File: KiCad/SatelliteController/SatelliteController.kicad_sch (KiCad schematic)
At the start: 35 parts, among them J1 CONN_ICSP, J13 CONN_7SEG, J2 CONN_USB, J3 USB_B_Micro, U1 FT232RL, U2 ATMEGA2560-16AUR, Y1 HUSG-16.000-20

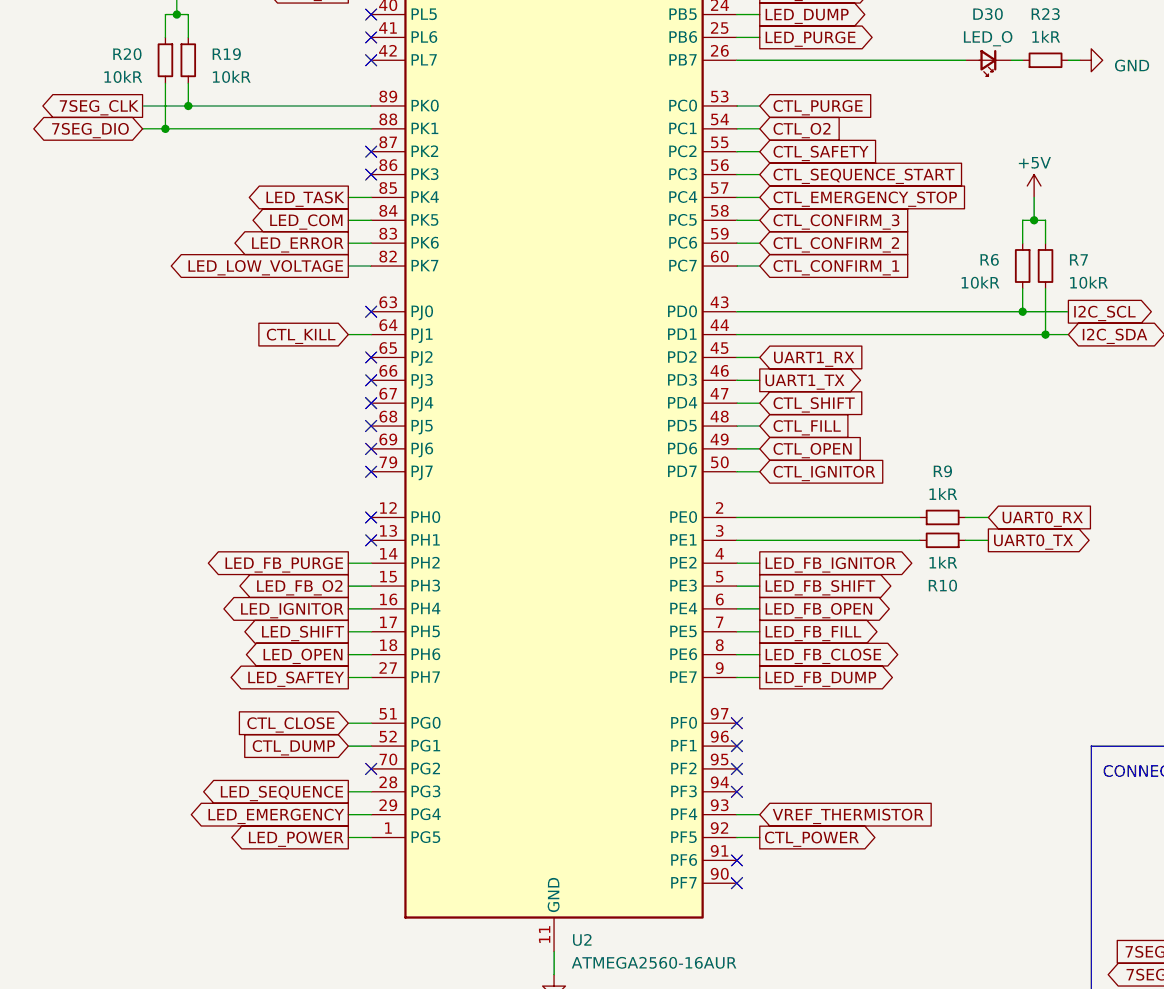
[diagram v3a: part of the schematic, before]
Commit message: 手動操作を削除
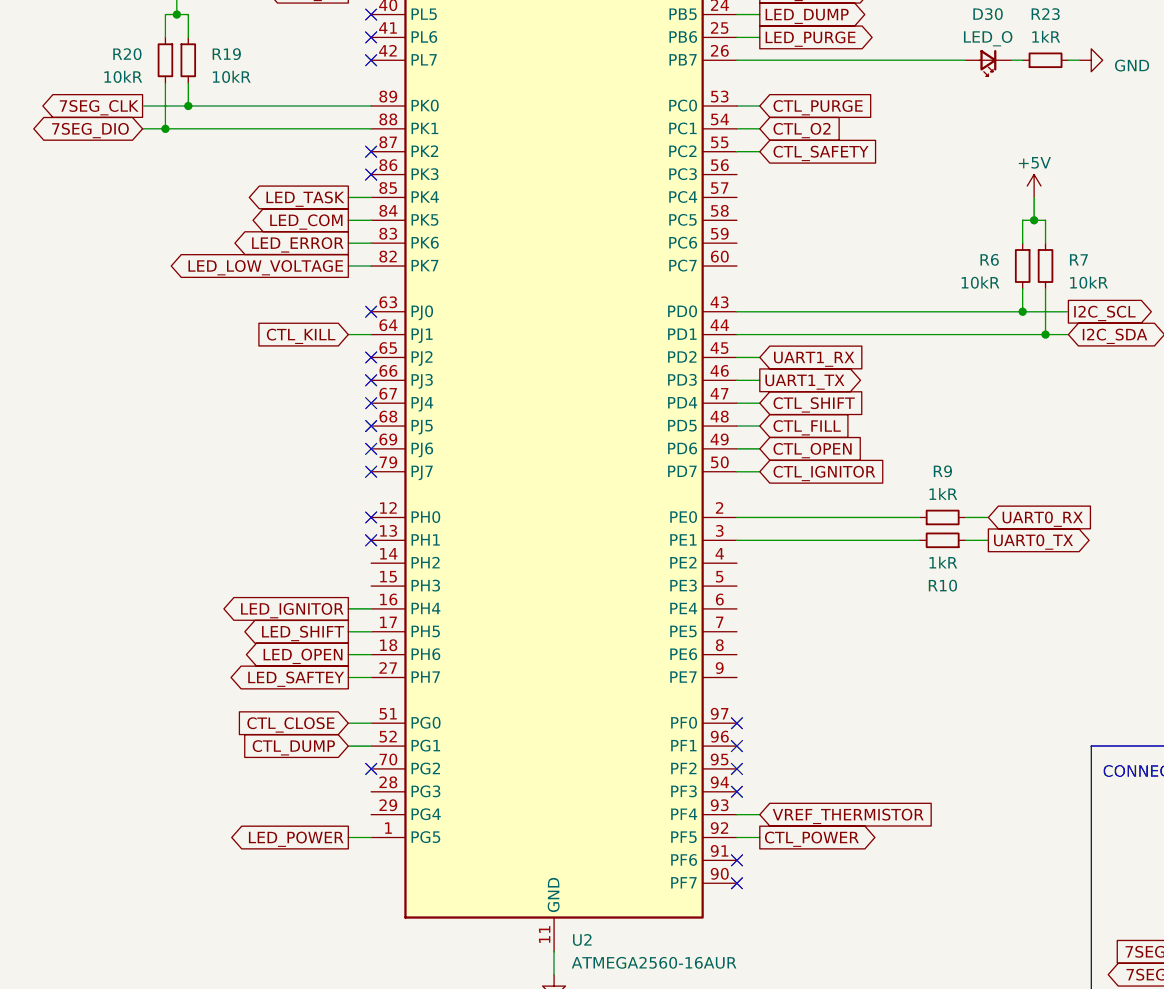
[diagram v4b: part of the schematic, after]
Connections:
- net CTL_CONFIRM_1: no longer names the net of U2.60 (PC7)
- net CTL_CONFIRM_2: no longer names the net of U2.59 (PC6)
- net CTL_CONFIRM_3: no longer names the net of U2.58 (PC5)
- net CTL_EMERGENCY_STOP: no longer names the net of U2.57 (PC4)
- net CTL_SEQUENCE_START: no longer names the net of U2.56 (PC3)
- net LED_EMERGENCY: no longer names the net of U2.29 (PG4)
- net LED_FB_CLOSE: no longer names the net of U2.8 (PE6)
- net LED_FB_DUMP: no longer names the net of U2.9 (PE7)
- net LED_FB_FILL: no longer names the net of U2.7 (PE5)
- net LED_FB_IGNITOR: no longer names the net of U2.4 (PE2)
- net LED_FB_O2: no longer names the net of U2.15 (PH3)
- net LED_FB_OPEN: no longer names the net of U2.6 (PE4)
- net LED_FB_PURGE: no longer names the net of U2.14 (PH2)
- net LED_FB_SHIFT: no longer names the net of U2.5 (PE3)
- net LED_SEQUENCE: no longer names the net of U2.28 (PG3)
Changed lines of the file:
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@@
-    (stroke (width 0) (type default))
-  )
-  (wire (pts (xy 52.07 147.32) (xy 54.61 147.32))
     (stroke (width 0) (type default))
   )
@@
     (stroke (width 0) (type default))
   )
-  (wire (pts (xy 95.25 154.94) (xy 97.79 154.94))
-    (stroke (width 0) (type default))
-  )
   (wire (pts (xy 240.03 38.1) (xy 242.57 38.1))
     (stroke (width 0) (type default))
@@
     (stroke (width 0) (type default))
   )
-  (wire (pts (xy 95.25 101.6) (xy 97.79 101.6))
-    (stroke (width 0) (type default))
-  )
   (wire (pts (xy 91.44 20.32) (xy 91.44 22.86))
     (stroke (width 0) (type default))
@@
     (stroke (width 0) (type default))
   )
-  (wire (pts (xy 95.25 104.14) (xy 97.79 104.14))
-    (stroke (width 0) (type default))
-  )
   (wire (pts (xy 95.25 71.12) (xy 97.79 71.12))
     (stroke (width 0) (type default))
   )
-  (wire (pts (xy 95.25 144.78) (xy 97.79 144.78))
-    (stroke (width 0) (type default))
-  )
   (wire (pts (xy 41.91 30.48) (xy 41.91 33.02))
     (stroke (width 0) (type default))
@@
     (stroke (width 0) (type default))
   )
-  (wire (pts (xy 95.25 147.32) (xy 97.79 147.32))
-    (stroke (width 0) (type default))
-  )
   (wire (pts (xy 95.25 121.92) (xy 97.79 121.92))
     (stroke (width 0) (type default))
@@
     (stroke (width 0) (type default))
   )
-  (wire (pts (xy 52.07 144.78) (xy 54.61 144.78))
-    (stroke (width 0) (type default))
-  )
-  (wire (pts (xy 95.25 109.22) (xy 97.79 109.22))
-    (stroke (width 0) (type default))
-  )
-  (wire (pts (xy 52.07 170.18) (xy 54.61 170.18))
-    (stroke (width 0) (type default))
-  )
   (wire (pts (xy 54.61 58.42) (xy 52.07 58.42))
     (stroke (width 0) (type default))
@@
     (stroke (width 0) (type default))
   )
-  (wire (pts (xy 95.25 149.86) (xy 97.79 149.86))
-    (stroke (width 0) (type default))
-  )
   (wire (pts (xy 172.72 58.42) (xy 172.72 55.88))
     (stroke (width 0) (type default))
@@
     (stroke (width 0) (type default))
   )
-  (wire (pts (xy 95.25 157.48) (xy 97.79 157.48))
-    (stroke (width 0) (type default))
-  )
   (wire (pts (xy 52.07 109.22) (xy 54.61 109.22))
     (stroke (width 0) (type default))
@@
     (stroke (width 0) (type default))
   )
-  (wire (pts (xy 95.25 111.76) (xy 97.79 111.76))
-    (stroke (width 0) (type default))
-  )
   (wire (pts (xy 196.85 71.12) (xy 196.85 81.28))
     (stroke (width 0) (type default))
   )
-  (wire (pts (xy 95.25 106.68) (xy 97.79 106.68))
-    (stroke (width 0) (type default))
-  )
   (wire (pts (xy 260.35 53.34) (xy 260.35 55.88))
     (stroke (width 0) (type default))
@@
     (stroke (width 0) (type default))
   )
-  (wire (pts (xy 95.25 152.4) (xy 97.79 152.4))
-    (stroke (width 0) (type default))
-  )
   (wire (pts (xy 31.75 96.52) (xy 29.21 96.52))
     (stroke (width 0) (type default))
@@
   )
   (wire (pts (xy 81.28 20.32) (xy 91.44 20.32))
-    (stroke (width 0) (type default))
-  )
-  (wire (pts (xy 52.07 172.72) (xy 54.61 172.72))
     (stroke (width 0) (type default))
   )
@@
     )
   )
-  (global_label "CTL_EMERGENCY_STOP" (shape input) (at 97.79 104.14 0) (fields_autoplaced)
-    (effects (font (size 1.27 1.27)) (justify left))
-    (property "Intersheetrefs" "${INTERSHEET_REFS}" (at 121.8018 104.14 0)
-      (effects (font (size 1.27 1.27)) (justify left) hide)
-    )
-  )
-  (global_label "CTL_SEQUENCE_START" (shape input) (at 97.79 101.6 0) (fields_autoplaced)
-    (effects (font (size 1.27 1.27)) (justify left))
-    (property "Intersheetrefs" "${INTERSHEET_REFS}" (at 121.318 101.6 0)
-      (effects (font (size 1.27 1.27)) (justify left) hide)
-    )
-  )
-  (global_label "CTL_CONFIRM_1" (shape input) (at 97.79 111.76 0) (fields_autoplaced)
-    (effects (font (size 1.27 1.27)) (justify left))
-    (property "Intersheetrefs" "${INTERSHEET_REFS}" (at 115.452 111.76 0)
-      (effects (font (size 1.27 1.27)) (justify left) hide)
-    )
-  )
-  (global_label "LED_FB_OPEN" (shape output) (at 97.79 149.86 0) (fields_autoplaced)
-    (effects (font (size 1.27 1.27)) (justify left))
-    (property "Intersheetrefs" "${INTERSHEET_REFS}" (at 113.5167 149.86 0)
-      (effects (font (size 1.27 1.27)) (justify left) hide)
-    )
-  )
   (global_label "LED_COM" (shape output) (at 52.07 106.68 180) (fields_autoplaced)
     (effects (font (size 1.27 1.27)) (justify right))
@@
     )
   )
-  (global_label "LED_FB_FILL" (shape output) (at 97.79 152.4 0) (fields_autoplaced)
-    (effects (font (size 1.27 1.27)) (justify left))
-    (property "Intersheetrefs" "${INTERSHEET_REFS}" (at 112.1863 152.4 0)
-      (effects (font (size 1.27 1.27)) (justify left) hide)
-    )
-  )
-  (global_label "LED_FB_PURGE" (shape output) (at 52.07 144.78 180) (fields_autoplaced)
-    (effects (font (size 1.27 1.27)) (justify right))
-    (property "Intersheetrefs" "${INTERSHEET_REFS}" (at 35.1338 144.78 0)
-      (effects (font (size 1.27 1.27)) (justify right) hide)
-    )
-  )
   (global_label "CTL_RS485_DERE" (shape output) (at 97.79 53.34 0) (fields_autoplaced)
     (effects (font (size 1.27 1.27)) (justify left))
@@
     )
   )
-  (global_label "LED_SEQUENCE" (shape output) (at 52.07 170.18 180) (fields_autoplaced)
-    (effects (font (size 1.27 1.27)) (justify right))
-    (property "Intersheetrefs" "${INTERSHEET_REFS}" (at 34.8315 170.18 0)
-      (effects (font (size 1.27 1.27)) (justify right) hide)
-    )
-  )
   (global_label "7SEG_DIO" (shape bidirectional) (at 148.59 190.5 180) (fields_autoplaced)
     (effects (font (size 1.27 1.27)) (justify right))
@@
     )
   )
-  (global_label "LED_FB_SHIFT" (shape output) (at 97.79 147.32 0) (fields_autoplaced)
-    (effects (font (size 1.27 1.27)) (justify left))
-    (property "Intersheetrefs" "${INTERSHEET_REFS}" (at 113.6377 147.32 0)
-      (effects (font (size 1.27 1.27)) (justify left) hide)
-    )
-  )
   (global_label "CTL_RESET" (shape output) (at 201.93 111.76 0) (fields_autoplaced)
     (effects (font (size 1.27 1.27)) (justify left))
@@
     )
   )
-  (global_label "LED_EMERGENCY" (shape output) (at 52.07 172.72 180) (fields_autoplaced)
-    (effects (font (size 1.27 1.27)) (justify right))
-    (property "Intersheetrefs" "${INTERSHEET_REFS}" (at 33.622 172.72 0)
-      (effects (font (size 1.27 1.27)) (justify right) hide)
-    )
-  )
-  (global_label "CTL_CONFIRM_3" (shape input) (at 97.79 106.68 0) (fields_autoplaced)
-    (effects (font (size 1.27 1.27)) (justify left))
-    (property "Intersheetrefs" "${INTERSHEET_REFS}" (at 115.452 106.68 0)
-      (effects (font (size 1.27 1.27)) (justify left) hide)
-    )
-  )
   (global_label "UART0_TX" (shape input) (at 242.57 38.1 0) (fields_autoplaced)
     (effects (font (size 1.27 1.27)) (justify left))
@@
     )
   )
-  (global_label "LED_FB_IGNITOR" (shape output) (at 97.79 144.78 0) (fields_autoplaced)
-    (effects (font (size 1.27 1.27)) (justify left))
-    (property "Intersheetrefs" "${INTERSHEET_REFS}" (at 115.8149 144.78 0)
-      (effects (font (size 1.27 1.27)) (justify left) hide)
-    )
-  )
   (global_label "7SEG_CLK" (shape output) (at 29.21 93.98 180) (fields_autoplaced)
     (effects (font (size 1.27 1.27)) (justify right))
@@
     )
   )
-  (global_label "LED_FB_O2" (shape output) (at 52.07 147.32 180) (fields_autoplaced)
-    (effects (font (size 1.27 1.27)) (justify right))
-    (property "Intersheetrefs" "${INTERSHEET_REFS}" (at 38.8833 147.32 0)
-      (effects (font (size 1.27 1.27)) (justify right) hide)
-    )
-  )
   (global_label "USB_D-" (shape bidirectional) (at 163.83 45.72 180) (fields_autoplaced)
     (effects (font (size 1.27 1.27)) (justify right))
@@
     )
   )
-  (global_label "LED_FB_DUMP" (shape output) (at 97.79 157.48 0) (fields_autoplaced)
-    (effects (font (size 1.27 1.27)) (justify left))
-    (property "Intersheetrefs" "${INTERSHEET_REFS}" (at 113.7586 157.48 0)
-      (effects (font (size 1.27 1.27)) (justify left) hide)
-    )
-  )
-  (global_label "LED_FB_CLOSE" (shape output) (at 97.79 154.94 0) (fields_autoplaced)
-    (effects (font (size 1.27 1.27)) (justify left))
-    (property "Intersheetrefs" "${INTERSHEET_REFS}" (at 114.4238 154.94 0)
-      (effects (font (size 1.27 1.27)) (justify left) hide)
-    )
-  )
   (global_label "USB_VBUS" (shape bidirectional) (at 234.95 130.81 180) (fields_autoplaced)
     (effects (font (size 1.27 1.27)) (justify right))
@@
     )
   )
-  (global_label "CTL_CONFIRM_2" (shape input) (at 97.79 109.22 0) (fields_autoplaced)
-    (effects (font (size 1.27 1.27)) (justify left))
-    (property "Intersheetrefs" "${INTERSHEET_REFS}" (at 115.452 109.22 0)
-      (effects (font (size 1.27 1.27)) (justify left) hide)
-    )
-  )

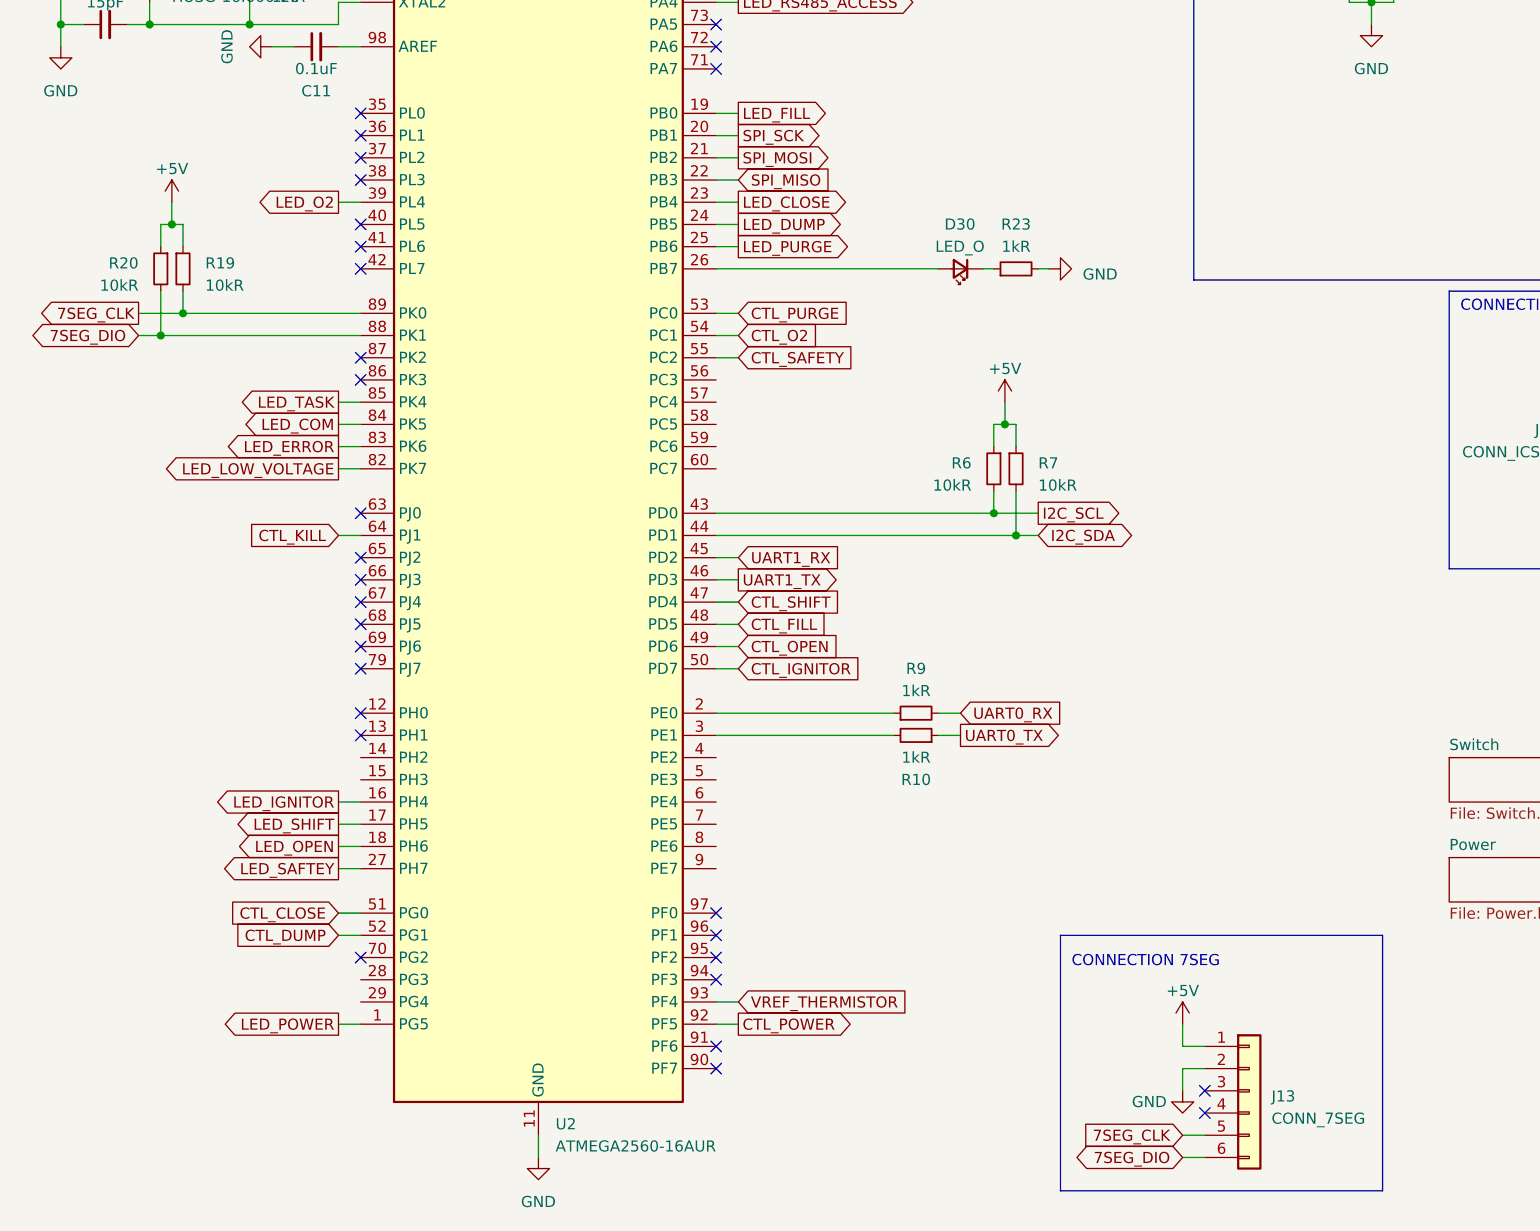
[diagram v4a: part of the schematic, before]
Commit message: 7セグ用コネクタを6Pから14Pの空いているピンに押し込んだ
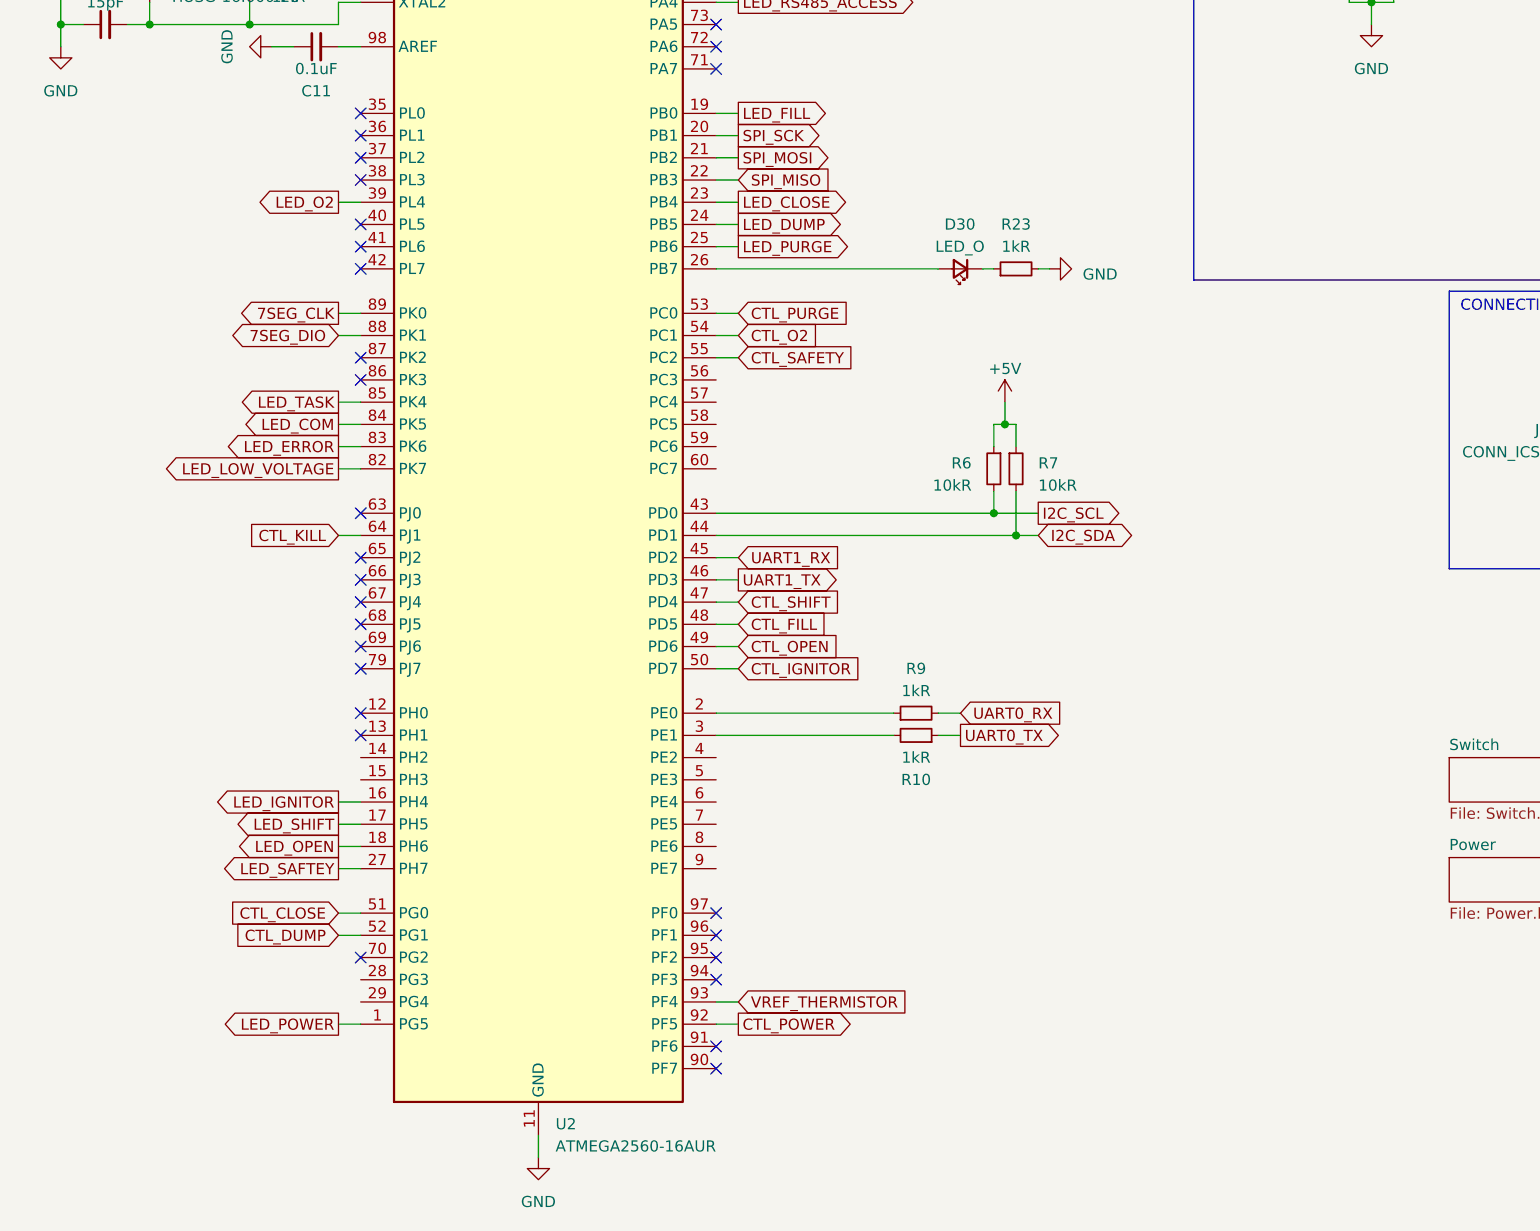
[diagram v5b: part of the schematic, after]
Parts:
- removed J13: CONN_7SEG, TSRP_Connector_Hirose:DF51A-6DP-2DSA, symbol Connector_Generic:Conn_01x06
- removed R19, R20: 10kR, Resistor_SMD:R_0603_1608Metric_Pad0.98x0.95mm_HandSolder, symbol Device:R_Small
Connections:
- no-connect marks 45 -> 43
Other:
- note removed: "CONNECTION 7SEG"

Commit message: 配線を避難させた
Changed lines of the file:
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@@
+    )
+  )
+  (global_label "VREF_N2O_PRESS" (shape input) (at 105.41 165.1 0) (fields_autoplaced)
+    (effects (font (size 1.27 1.27)) (justify left))
+    (property "Intersheetrefs" "${INTERSHEET_REFS}" (at 124.8257 165.1 0)
+      (effects (font (size 1.27 1.27)) (justify left) hide)
     )
   )
